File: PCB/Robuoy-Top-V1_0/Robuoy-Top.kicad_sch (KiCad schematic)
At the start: 6 parts

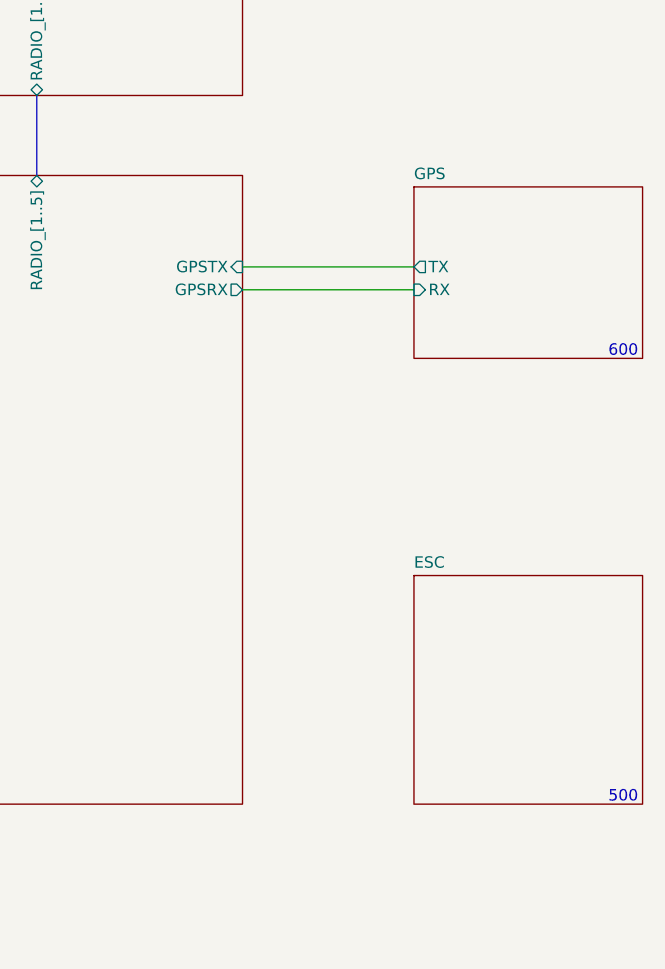
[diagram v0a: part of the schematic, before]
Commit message: Directory renamed. Top finished Sub started
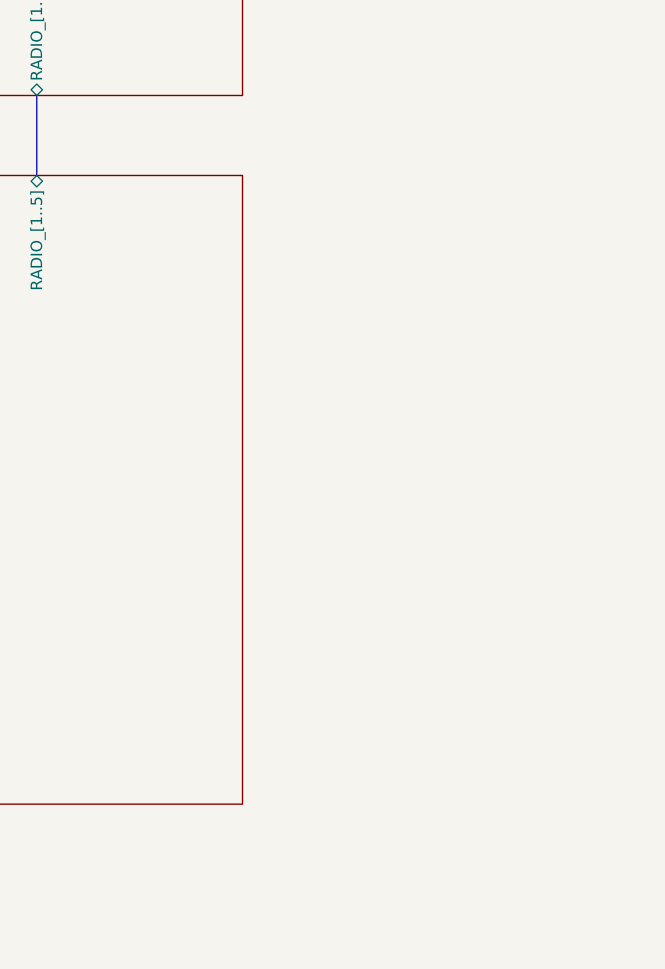
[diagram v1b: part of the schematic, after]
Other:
- removed sheet ESC
- removed sheet GPS
- sheet CPU ports: added none; removed GPSRX, GPSTX
- note removed: "500"
- note removed: "600"
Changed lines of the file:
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@@
 		(at 45.72 191.77)
-	)
-	(wire
-		(pts
-			(xy 139.7 60.96) (xy 158.75 60.96)
-		)
-		(stroke
-			(width 0)
-			(type default)
-		)
 	)
 	(bus
 		(pts
 			(xy 116.84 41.91) (xy 116.84 50.8)
-		)
-		(stroke
-			(width 0)
-			(type default)
-		)
-	)
-	(wire
-		(pts
-			(xy 139.7 63.5) (xy 158.75 63.5)
 		)
 		(stroke
@@
 		)
 	)
-	(text "600"
-		(exclude_from_sim no)
-		(at 180.34 71.12 0)
-		(effects
-			(font
-				(size 1.27 1.27)
-			)
-			(justify left bottom)
-		)
-	)
 	(text "ESP32\nLORA\nGPS\nCOMPASS\nGIRO\nACCELOROMETER\nBATTERY MONITOR\nPOWERSUPPY 12V 5V 3.3V\nMODE SWITCH\nLEDSTRIP\nLipo monitoring\n"
 		(exclude_from_sim no)
@@
 		(exclude_from_sim no)
 		(at 95.25 41.91 0)
-		(effects
-			(font
-				(size 1.27 1.27)
-			)
-			(justify left bottom)
-		)
-	)
-	(text "500"
-		(exclude_from_sim no)
-		(at 180.34 120.65 0)
 		(effects
 			(font
@@
 		)
 		(instances
-			(project "Robuoy"
+			(project "Robuoy-Top"
 				(path "/77bea089-a6ae-4a6f-b95b-7a9010ad7c5d"
 					(reference "TP2")
@@
 		)
 		(instances
-			(project "Robuoy"
+			(project "Robuoy-Top"
 				(path "/77bea089-a6ae-4a6f-b95b-7a9010ad7c5d"
 					(reference "H1004")
@@
 		)
 		(instances
-			(project "Robuoy"
+			(project "Robuoy-Top"
 				(path "/77bea089-a6ae-4a6f-b95b-7a9010ad7c5d"
 					(reference "H1003")
@@
 		)
 		(instances
-			(project "Robuoy"
+			(project "Robuoy-Top"
 				(path "/77bea089-a6ae-4a6f-b95b-7a9010ad7c5d"
 					(reference "TP1")
@@
 		)
 		(instances
-			(project "Robuoy"
+			(project "Robuoy-Top"
 				(path "/77bea089-a6ae-4a6f-b95b-7a9010ad7c5d"
 					(reference "H1002")
@@
 		)
 		(instances
-			(project "Robuoy"
+			(project "Robuoy-Top"
 				(path "/77bea089-a6ae-4a6f-b95b-7a9010ad7c5d"
 					(reference "H1001")
@@
 		)
 		(instances
-			(project "Robuoy"
+			(project "Robuoy-Top"
 				(path "/77bea089-a6ae-4a6f-b95b-7a9010ad7c5d"
 					(page "6")
@@
 			)
 		)
-		(pin "GPSRX" output
-			(at 139.7 63.5 0)
-			(effects
-				(font
-					(size 1.27 1.27)
-				)
-				(justify right)
-			)
-		)
-		(pin "GPSTX" input
-			(at 139.7 60.96 0)
-			(effects
-				(font
-					(size 1.27 1.27)
-				)
-				(justify right)
-			)
-		)
 		(pin "RADIO_[1..5]" bidirectional
 			(at 116.84 50.8 90)
@@
 		)
 		(instances
-			(project "Robuoy"
+			(project "Robuoy-Top"
 				(path "/77bea089-a6ae-4a6f-b95b-7a9010ad7c5d"
 					(page "1")
-				)
-			)
-		)
-	)
-	(sheet
-		(at 158.75 52.07)
-		(size 25.4 19.05)
-		(fields_autoplaced yes)
-		(stroke
-			(width 0.1524)
-			(type solid)
-		)
-		(fill
-			(color 0 0 0 0.0000)
-		)
-		(property "Sheetname" "GPS"
-			(at 158.75 51.3584 0)
-			(effects
-				(font
-					(size 1.27 1.27)
-				)
-				(justify left bottom)
-			)
-		)
-		(property "Sheetfile" "Gps_sch.kicad_sch"
-			(at 158.75 71.7046 0)
-			(effects
-				(font
-					(size 1.27 1.27)
-				)
-				(justify left top)
-				(hide yes)
-			)
-		)
-		(pin "RX" input
-			(at 158.75 63.5 180)
-			(effects
-				(font
-					(size 1.27 1.27)
-				)
-				(justify left)
-			)
-		)
-		(pin "TX" output
-			(at 158.75 60.96 180)
-			(effects
-				(font
-					(size 1.27 1.27)
-				)
-				(justify left)
-			)
-		)
-		(instances
-			(project "Robuoy"
-				(path "/77bea089-a6ae-4a6f-b95b-7a9010ad7c5d"
-					(page "5")
 				)
 			)
@@
 		)
 		(instances
-			(project "Robuoy"
+			(project "Robuoy-Top"
 				(path "/77bea089-a6ae-4a6f-b95b-7a9010ad7c5d"
 					(page "2")
 				)
 			)
-		)
-	)
-	(sheet
-		(at 158.75 95.25)
-		(size 25.4 25.4)
-		(fields_autoplaced yes)
-		(stroke
-			(width 0.1524)
-			(type solid)
-		)
-		(fill
-			(color 0 0 0 0.0000)
-		)
-		(property "Sheetname" "ESC"
-			(at 158.75 94.5384 0)
-			(effects
-				(font
-					(size 1.27 1.27)
-				)
-				(justify left bottom)
-			)
-		)
-		(property "Sheetfile" "Esc_sch.kicad_sch"
-			(at 158.75 121.2346 0)
-			(effects
-				(font
-					(size 1.27 1.27)
-				)
-				(justify left top)
-				(hide yes)
-			)
-		)
-		(instances
-			(project "Robuoy"
-				(path "/77bea089-a6ae-4a6f-b95b-7a9010ad7c5d"
-					(page "4")
-				)
-			)

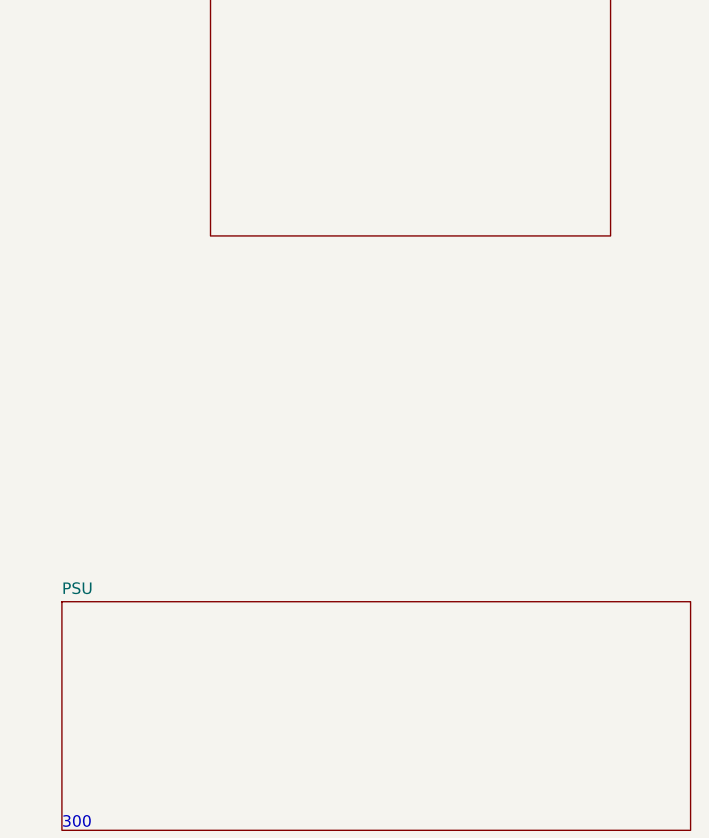
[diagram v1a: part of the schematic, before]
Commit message: Sub ready for routing
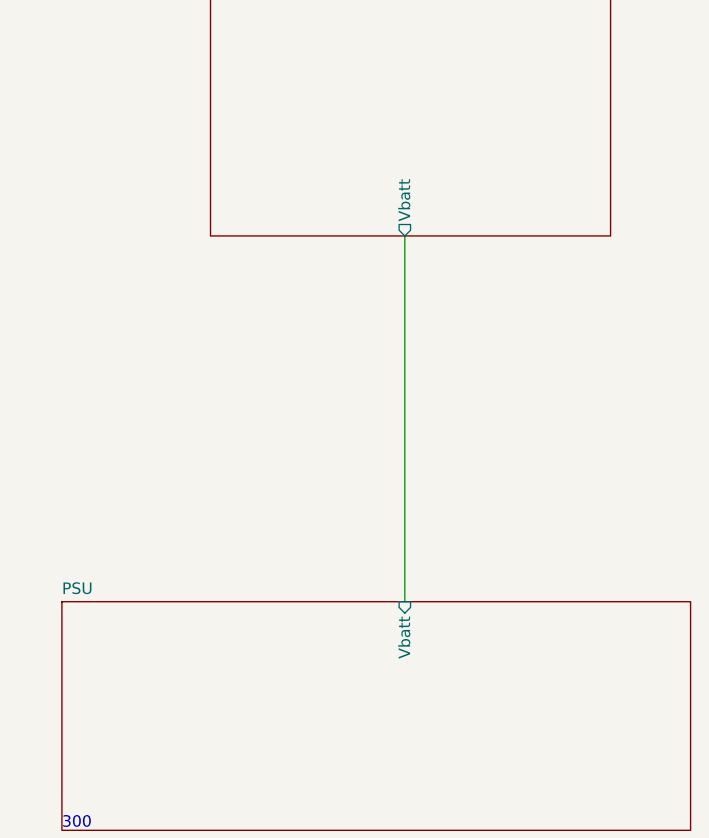
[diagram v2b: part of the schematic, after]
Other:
- sheet CPU ports: added Vbatt; removed none
- sheet PSU ports: added Vbatt; removed none
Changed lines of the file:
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@@
 		(at 45.72 191.77)
+	)
+	(wire
+		(pts
+			(xy 116.84 120.65) (xy 116.84 161.29)
+		)
+		(stroke
+			(width 0)
+			(type default)
+		)
 	)
 	(bus
@@
 			)
 		)
+		(pin "Vbatt" output
+			(at 116.84 120.65 270)
+			(effects
+				(font
+					(size 1.27 1.27)
+				)
+				(justify left)
+			)
+		)
 		(instances
 			(project "Robuoy-Top"
@@
 			)
 		)
+		(pin "Vbatt" input
+			(at 116.84 161.29 90)
+			(effects
+				(font
+					(size 1.27 1.27)
+				)
+				(justify right)
+			)
+		)

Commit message: gETTING READY FOR ROUTING
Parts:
- renumbered H1001 to H401, H1002 to H402, H1003 to H403, H1004 to H404, TP1 to TP401, TP2 to TP402
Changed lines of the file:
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@@
 		(dnp no)
 		(fields_autoplaced yes)
-		(property "Reference" "TP2"
+		(property "Reference" "TP402"
 			(at 46.99 190.5 0)
 			(effects
@@
 			(project "Robuoy-Top"
 				(path "/77bea089-a6ae-4a6f-b95b-7a9010ad7c5d"
-					(reference "TP2")
+					(reference "TP402")
 					(unit 1)
 				)
@@
 		(on_board yes)
 		(dnp no)
-		(property "Reference" "H1004"
+		(property "Reference" "H404"
 			(at 27.94 187.96 0)
 			(effects
@@
 			(project "Robuoy-Top"
 				(path "/77bea089-a6ae-4a6f-b95b-7a9010ad7c5d"
-					(reference "H1004")
+					(reference "H404")
 					(unit 1)
 				)
@@
 		(on_board yes)
 		(dnp no)
-		(property "Reference" "H1003"
+		(property "Reference" "H403"
 			(at 24.13 185.42 0)
 			(effects
@@
 			(project "Robuoy-Top"
 				(path "/77bea089-a6ae-4a6f-b95b-7a9010ad7c5d"
-					(reference "H1003")
+					(reference "H403")
 					(unit 1)
 				)
@@
 		(dnp no)
 		(fields_autoplaced yes)
-		(property "Reference" "TP1"
+		(property "Reference" "TP401"
 			(at 38.1 190.5 0)
 			(effects
@@
 			(project "Robuoy-Top"
 				(path "/77bea089-a6ae-4a6f-b95b-7a9010ad7c5d"
-					(reference "TP1")
+					(reference "TP401")
 					(unit 1)
 				)
@@
 		(on_board yes)
 		(dnp no)
-		(property "Reference" "H1002"
+		(property "Reference" "H402"
 			(at 19.05 187.96 0)
 			(effects
@@
 			(project "Robuoy-Top"
 				(path "/77bea089-a6ae-4a6f-b95b-7a9010ad7c5d"
-					(reference "H1002")
+					(reference "H402")
 					(unit 1)
 				)
@@
 		(on_board yes)
 		(dnp no)
-		(property "Reference" "H1001"
+		(property "Reference" "H401"
 			(at 13.97 185.42 0)
 			(effects
@@
 			(project "Robuoy-Top"
 				(path "/77bea089-a6ae-4a6f-b95b-7a9010ad7c5d"
-					(reference "H1001")
-					(unit 1)
-				)
+					(reference "H401")
+					(unit 1)
+				)

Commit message: Some more routing
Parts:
- removed TP401: RW1, A_Misc:ReworkPins, symbol Connector:TestPoint_Small
- removed TP402: RW2, A_Misc:ReworkPins, symbol Connector:TestPoint_Small
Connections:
- no-connect marks 2 -> 0
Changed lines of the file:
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@@
 		(company "NicE Engineering")
-	)
-	(no_connect
-		(at 36.83 191.77)
-	)
-	(no_connect
-		(at 45.72 191.77)
 	)
 	(wire
@@
 			)
 			(justify left bottom)
-		)
-	)
-	(symbol
-		(lib_id "Connector:TestPoint_Small")
-		(at 45.72 191.77 0)
-		(unit 1)
-		(exclude_from_sim no)
-		(in_bom no)
-		(on_board yes)
-		(dnp no)
-		(fields_autoplaced yes)
-		(property "Reference" "TP402"
-			(at 46.99 190.5 0)
-			(effects
-				(font
-					(size 1.27 1.27)
-				)
-				(justify left)
-			)
-		)
-		(property "Value" "RW2"
-			(at 46.99 193.04 0)
-			(effects
-				(font
-					(size 1.27 1.27)
-				)
-				(justify left)
-			)
-		)
-		(property "Footprint" "A_Misc:ReworkPins"
-			(at 50.8 191.77 0)
-			(effects
-				(font
-					(size 1.27 1.27)
-				)
-				(hide yes)
-			)
-		)
-		(property "Datasheet" "~"
-			(at 50.8 191.77 0)
-			(effects
-				(font
-					(size 1.27 1.27)
-				)
-				(hide yes)
-			)
-		)
-		(property "Description" ""
-			(at 45.72 191.77 0)
-			(effects
-				(font
-					(size 1.27 1.27)
-				)
-				(hide yes)
-			)
-		)
-		(property "JLCS" ""
-			(at 45.72 191.77 0)
-			(effects
-				(font
-					(size 1.27 1.27)
-				)
-				(hide yes)
-			)
-		)
-		(pin "1"
-		)
-		(instances
-			(project "Robuoy-Top"
-				(path "/77bea089-a6ae-4a6f-b95b-7a9010ad7c5d"
-					(reference "TP402")
-					(unit 1)
-				)
-			)
 		)
 	)
@@
 					(unit 1)
 				)
-			)
-		)
-	)
-	(symbol
-		(lib_id "Connector:TestPoint_Small")
-		(at 36.83 191.77 0)
-		(unit 1)
-		(exclude_from_sim no)
-		(in_bom no)
-		(on_board yes)
-		(dnp no)
-		(fields_autoplaced yes)
-		(property "Reference" "TP401"
-			(at 38.1 190.5 0)
-			(effects
-				(font
-					(size 1.27 1.27)
-				)
-				(justify left)
-			)
-		)
-		(property "Value" "RW1"
-			(at 38.1 193.04 0)
-			(effects
-				(font
-					(size 1.27 1.27)
-				)
-				(justify left)
-			)
-		)
-		(property "Footprint" "A_Misc:ReworkPins"
-			(at 41.91 191.77 0)
-			(effects
-				(font
-					(size 1.27 1.27)
-				)
-				(hide yes)
-			)
-		)
-		(property "Datasheet" "~"
-			(at 41.91 191.77 0)
-			(effects
-				(font
-					(size 1.27 1.27)
-				)
-				(hide yes)
-			)
-		)
-		(property "Description" ""
-			(at 36.83 191.77 0)
-			(effects
-				(font
-					(size 1.27 1.27)
-				)
-				(hide yes)
-			)
-		)
-		(property "JLCS" ""
-			(at 36.83 191.77 0)
-			(effects
-				(font
-					(size 1.27 1.27)
-				)
-				(hide yes)
-			)
-		)
-		(pin "1"
-		)
-		(instances
-			(project "Robuoy-Top"
-				(path "/77bea089-a6ae-4a6f-b95b-7a9010ad7c5d"
-					(reference "TP401")
-					(unit 1)
-				)
